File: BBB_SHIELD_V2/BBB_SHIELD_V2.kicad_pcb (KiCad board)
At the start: 4 copper layers, 89.3 x 102.1 mm, 120 parts, among them J1 Screw_Terminal_01x04, J2 Conn_01x06_Male, J3 Conn_01x06_Male, J4 Conn_01x10_Female, P12V1 VX78XX, P5V1 VX78XX, P8 BBCONN, P9 BBCONN, Q1 Q_NMOS_GDS, U1 LTC7004, U4 INA138, U5 OPA340NA

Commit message: Rev 2 problem fixes.
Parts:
- removed TPFETOUT1: TestPoint, TestPoint:TestPoint_THTPad_D1.0mm_Drill0.5mm
- added C46: 180uF,50V, Capacitor_THT:CP_Radial_D8.0mm_P3.50mm, F.Cu at (184.8, 138.9)
- added C47: 180uF,50V, Capacitor_THT:CP_Radial_D8.0mm_P3.50mm, F.Cu at (184.8, 130.2)
- added C48: 180uF,50V, Capacitor_THT:CP_Radial_D8.0mm_P3.50mm, F.Cu at (184.8, 121.5)
- added C49: 1uF, Capacitor_SMD:C_0805_2012Metric, F.Cu at (135.3, 129.4)
- added R22: 0, Resistor_SMD:R_0805_2012Metric, F.Cu at (155.9, 103.6)
- added R25: 0, Resistor_SMD:R_0805_2012Metric, F.Cu at (152.8, 81.4)
- added R26: 200, Resistor_SMD:R_0805_2012Metric, F.Cu at (135.3, 126.5)
- C1: value 1nF -> 0.1uF
- C2: value 0.1uF -> 1uF
- C45: value C -> 1uF
- D4: value LEDHMI1 -> LED
- D5: value LEDHMI2 -> LED
- D6: value LEDHMI3 -> LED
- D7: value LEDHMI4 -> LED
- D8: value LEDHTBT -> LED
- R1, R2, R3, R4: value 1K0 -> 1K
- R18, R19: value 5K6 -> 4K7
- R20: value 100R -> 4K7
- R21: value 100R -> 200R
- R23: value 100R -> 1K
- R24: value 24K9 -> 49K9
- R5: value 910R -> 1K
- R6: value 23K2 -> 49K9
- R8: value 2K49 -> 4K7
- TP1, TP2: footprint TestPoint:TestPoint_THTPad_D1.0mm_Drill0.5mm -> Connector_PinHeader_1.27mm:PinHeader_1x02_P1.27mm_Vertical
- moved TP2 26.4 mm to (132.0, 110.6), turned to 270 degrees
- moved TP1 7.22 mm to (191.0, 114.6)
- moved C2 3.37 mm to (139.0, 127.9)
- moved D3 3.35 mm to (143.4, 127.9)
- moved P12V1 3.19 mm to (170.8, 124.7)
- moved P5V1 2.83 mm to (170.8, 136.7)
- moved C3 2.12 mm to (143.4, 124.8)
- moved TP5V1 1.96 mm to (178.2, 141.7)
- moved TP12V1 0.99 mm to (178.1, 127.7)
- moved CONN5V5 0.60 mm to (112.5, 101.3)
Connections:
- CONN5V5 pad 2: _VDD_5V_PROT -> _VDD_3V3
- PIC1 pad 15: Net-(PIC1-Pad15) -> GND
- PIC1 pad 17: Net-(PIC1-Pad17) -> /BB_HEADERS/SCL1
- PIC1 pad 18: /BB_HEADERS/SCL1 -> /BB_HEADERS/SDA1
- PIC1 pad 19: /BB_HEADERS/SDA1 -> Net-(PIC1-Pad19)
- TP2 pad 1: _VDD_24V_PROT -> GND
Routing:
- net Net-(PIC1-Pad19): track 0.00 -> 27.1 mm, vias 0 -> 4
- net _VDD_3V3: track 61.4 -> 84.9 mm
- net _VDD_5V_PROT: track 128.6 -> 150.7 mm, vias 2 -> 4
- net Net-(PIC1-Pad11): track 0.00 -> 14.7 mm, vias 0 -> 3
- net /FET/FET_OUT: track 52.3 -> 40.5 mm
- net _PWR_BUTT: track 37.9 -> 48.0 mm, vias 2 -> 4
- net _SYS_RESETn: track 48.6 -> 57.2 mm, vias 2 -> 3
- net Net-(C49-Pad1): track 0.00 -> 4.57 mm
- net _VDD_12V_PROT: track 58.6 -> 55.5 mm
- net Net-(Q1-Pad1): track 20.5 -> 23.4 mm
- net GND: track 119.6 -> 122.2 mm, vias 69 -> 71
- net /CONTROLLER/3V3_REF: track 64.7 -> 62.7 mm, vias 4 -> 5
- net /BB_HEADERS/SDA1: track 71.2 -> 73.0 mm, vias 4 -> 6
- net /POWER_PROTECTION/VDD_24V: track 12.3 -> 14.1 mm
- net Net-(C2-Pad1): track 12.1 -> 11.1 mm, vias 3 -> 2
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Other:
- board text added: "3.3V P9[3,4]"
- board text added: "5V P9[5,6]"
- board text added: "REV: 3"
- board text added: "TP24V"
- board text added: "TPFET"
- board text added: "TPISEN"
- board text removed: "5V UNFUSED P9 [5,6]"
- board text removed: "TPFETDRV"
- board text removed: "TPISENSE"

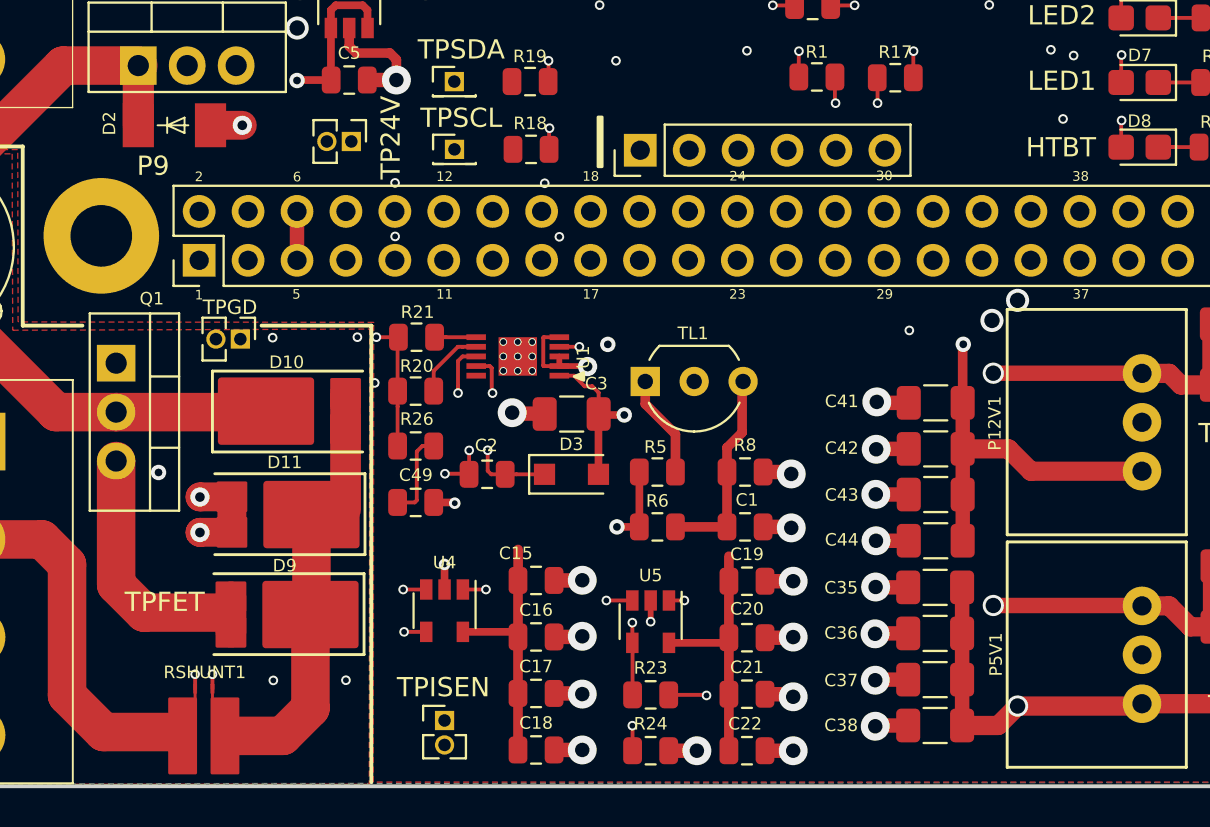
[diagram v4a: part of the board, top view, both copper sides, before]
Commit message: Schematics cleanup.  Gerbers for the latest manufacturing release.
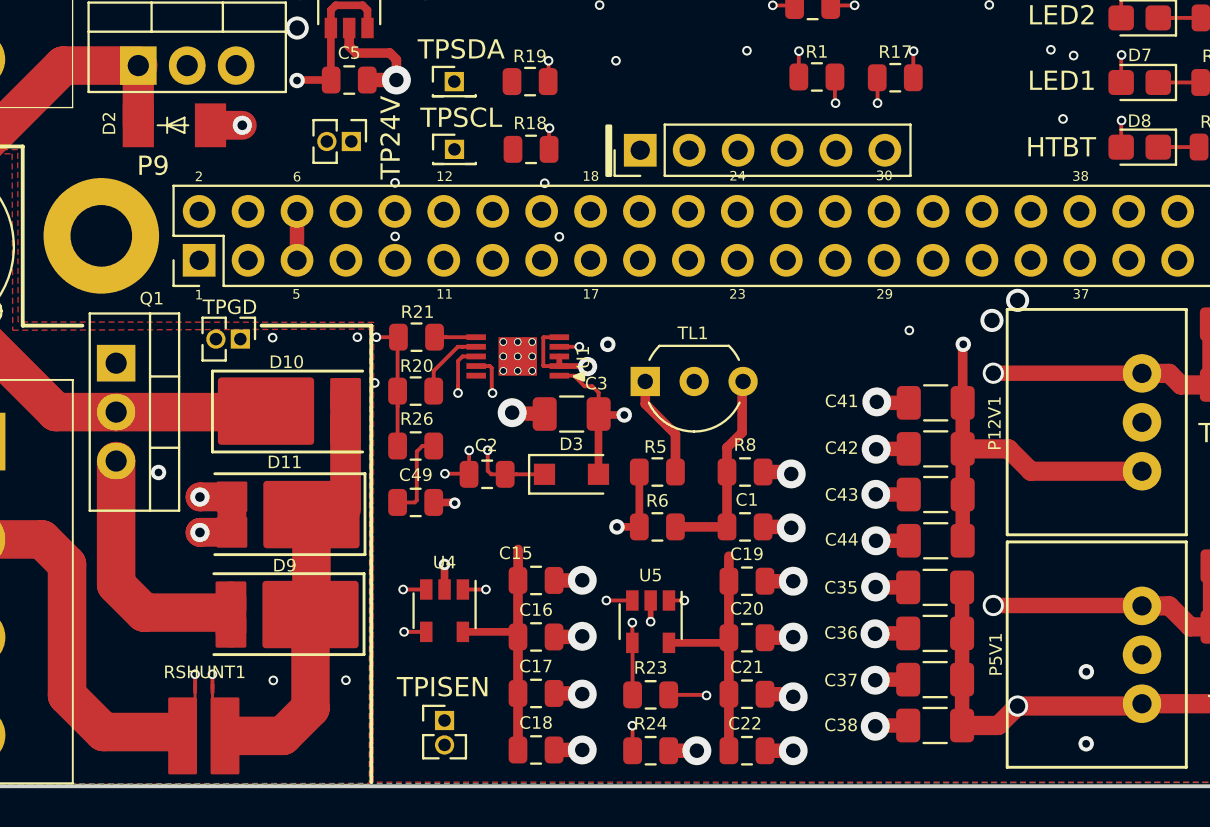
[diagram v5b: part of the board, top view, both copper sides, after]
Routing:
- net _VDD_3V3: track 84.9 -> 88.8 mm, vias 0 -> 2
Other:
- board text removed: "TPFET"
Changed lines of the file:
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@@
   (general
     (thickness 1.6)
-    (drawings 107)
-    (tracks 1365)
+    (drawings 106)
+    (tracks 1373)
     (zones 0)
     (modules 126)
@@
       (drillshape 0)
       (scaleselection 1)
-      (outputdirectory "GERBER_2.1/"))
+      (outputdirectory "GERBER_3.0/"))
   )
   (net 0 "")
@@
     (effects (font (size 1 1) (thickness 0.2)))
   )
-  (gr_poly (pts (xy 144.98 111.95) (xy 144.77 111.95) (xy 144.77 109.37) (xy 144.98 109.37)) (layer F.SilkS) (width 0.15))
+  (gr_poly (pts (xy 145.43 112.41) (xy 145.22 112.41) (xy 145.22 109.83) (xy 145.43 109.83)) (layer F.SilkS) (width 0.15))
   (gr_poly (pts (xy 191.85 73.36) (xy 188.46 73.36) (xy 188.46 73.06) (xy 191.85 73.06)) (layer F.SilkS) (width 0.15))
   (gr_poly (pts (xy 191.9 92.61) (xy 188.51 92.61) (xy 188.51 92.31) (xy 191.9 92.31)) (layer F.SilkS) (width 0.15))
@@
     (effects (font (size 1 1) (thickness 0.1)))
   )
-  (gr_text TPFET (at 122.27 134.55) (layer F.SilkS)
-    (effects (font (size 1 1) (thickness 0.1)))
-  )
   (dimension 102.30044 (width 0.1) (layer B.Fab)
     (gr_text "102.300 mm" (at 196.850854 93.04032 270.1680223) (layer B.Fab)
@@
   (segment (start 112.5 106.98) (end 112.49 106.99) (width 0.75) (layer In1.Cu) (net 3))
   (segment (start 112.49 110.35) (end 112.49 106.38) (width 0.75) (layer In1.Cu) (net 3))
+  (segment (start 170.110001 138.810001) (end 170.110001 138.725685) (width 0.4) (layer In1.Cu) (net 3))
+  (via (at 170.12 138.170001) (size 0.8) (drill 0.4) (layers F.Cu B.Cu) (net 3))
+  (segment (start 170.110001 138.18) (end 170.12 138.170001) (width 0.4) (layer In1.Cu) (net 3))
+  (segment (start 170.110001 138.725685) (end 170.110001 138.18) (width 0.4) (layer In1.Cu) (net 3))
+  (segment (start 170.12 138.82) (end 170.110001 138.810001) (width 0.4) (layer In1.Cu) (net 3))
+  (via (at 170.110002 141.91) (size 0.8) (drill 0.4) (layers F.Cu B.Cu) (net 3))
+  (segment (start 170.110002 141.344315) (end 170.110002 141.91) (width 0.4) (layer In1.Cu) (net 3))
+  (segment (start 170.110001 138.725685) (end 170.110002 141.344315) (width 0.4) (layer In1.Cu) (net 3))
   (via (at 172.34 70.76) (size 0.5) (drill 0.3) (layers F.Cu B.Cu) (net 4))
   (segment (start 172.3375 72.35) (end 172.3375 70.7625) (width 0.2) (layer F.Cu) (net 4))
@@
     (connect_pads (clearance 0.2))
     (min_thickness 0.2)
-    (fill yes (arc_segments 32) (thermal_gap 0.25) (thermal_bridge_width 0.38) (smoothing fillet) (radius 0.5))
+    (fill yes (arc_segments 32) (thermal_gap 0.25) (thermal_bridge_width 0.4) (smoothing fillet) (radius 0.5))
     (polygon
       (pts
@@
     (connect_pads (clearance 0.2))
     (min_thickness 0.2)
-    (fill yes (arc_segments 32) (thermal_gap 0.25) (thermal_bridge_width 0.38) (smoothing fillet) (radius 0.5))
+    (fill yes (arc_segments 32) (thermal_gap 0.25) (thermal_bridge_width 0.4) (smoothing fillet) (radius 0.5))
     (polygon
       (pts
